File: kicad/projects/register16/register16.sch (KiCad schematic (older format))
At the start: 42 parts, among them J1 INPUT_ENABLE, J10 LOW, J2 OUTPUT_ENABLE, J3 CONTENTS, J4 Control_signal_backplane, J5 Aux_connection, J6 Bus_connection, J7 HIGH, J8 LOW, J9 HIGH, U1 74HCT04, U2 74HCT377, U3 74HCT377, U4 74HCT245, U5 74HCT245, U6 74HCT245, U7 74HCT245

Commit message: Register mostly complete
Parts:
- D1, D10, D11, D12, D13, D14, D15, D16, D2, D3, D4, D5, D6, D7, D8, D9: footprint LED_THT:LED_D5.0mm_Horizontal_O3.81mm_Z3.0mm -> eight-bit-computer:LED_D5.0mm_Horizontal_O3.81mm_Z3.0mm
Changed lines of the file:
@@
 F 0 "D15" H 8500 2850 50  0000 C CNN
 F 1 "LED" H 8300 2850 50  0000 C CNN
-F 2 "LED_THT:LED_D5.0mm_Horizontal_O3.81mm_Z3.0mm" H 8750 2900 50  0001 C CNN
+F 2 "eight-bit-computer:LED_D5.0mm_Horizontal_O3.81mm_Z3.0mm" H 8750 2900 50  0001 C CNN
 F 3 "~" H 8750 2900 50  0001 C CNN
 	1    8750 2900
@@
 F 0 "D16" H 8500 3000 50  0000 C CNN
 F 1 "LED" H 8300 3000 50  0000 C CNN
-F 2 "LED_THT:LED_D5.0mm_Horizontal_O3.81mm_Z3.0mm" H 8750 3050 50  0001 C CNN
+F 2 "eight-bit-computer:LED_D5.0mm_Horizontal_O3.81mm_Z3.0mm" H 8750 3050 50  0001 C CNN
 F 3 "~" H 8750 3050 50  0001 C CNN
 	1    8750 3050
@@
 F 0 "D13" H 8500 2550 50  0000 C CNN
 F 1 "LED" H 8300 2550 50  0000 C CNN
-F 2 "LED_THT:LED_D5.0mm_Horizontal_O3.81mm_Z3.0mm" H 8750 2600 50  0001 C CNN
+F 2 "eight-bit-computer:LED_D5.0mm_Horizontal_O3.81mm_Z3.0mm" H 8750 2600 50  0001 C CNN
 F 3 "~" H 8750 2600 50  0001 C CNN
 	1    8750 2600
@@
 F 0 "D14" H 8500 2700 50  0000 C CNN
 F 1 "LED" H 8300 2700 50  0000 C CNN
-F 2 "LED_THT:LED_D5.0mm_Horizontal_O3.81mm_Z3.0mm" H 8750 2750 50  0001 C CNN
+F 2 "eight-bit-computer:LED_D5.0mm_Horizontal_O3.81mm_Z3.0mm" H 8750 2750 50  0001 C CNN
 F 3 "~" H 8750 2750 50  0001 C CNN
 	1    8750 2750
@@
 F 0 "D11" H 8500 2250 50  0000 C CNN
 F 1 "LED" H 8300 2250 50  0000 C CNN
-F 2 "LED_THT:LED_D5.0mm_Horizontal_O3.81mm_Z3.0mm" H 8750 2300 50  0001 C CNN
+F 2 "eight-bit-computer:LED_D5.0mm_Horizontal_O3.81mm_Z3.0mm" H 8750 2300 50  0001 C CNN
 F 3 "~" H 8750 2300 50  0001 C CNN
 	1    8750 2300
@@
 F 0 "D12" H 8500 2400 50  0000 C CNN
 F 1 "LED" H 8300 2400 50  0000 C CNN
-F 2 "LED_THT:LED_D5.0mm_Horizontal_O3.81mm_Z3.0mm" H 8750 2450 50  0001 C CNN
+F 2 "eight-bit-computer:LED_D5.0mm_Horizontal_O3.81mm_Z3.0mm" H 8750 2450 50  0001 C CNN
 F 3 "~" H 8750 2450 50  0001 C CNN
 	1    8750 2450
@@
 F 0 "D9" H 8500 1950 50  0000 C CNN
 F 1 "LED" H 8300 1950 50  0000 C CNN
-F 2 "LED_THT:LED_D5.0mm_Horizontal_O3.81mm_Z3.0mm" H 8750 2000 50  0001 C CNN
+F 2 "eight-bit-computer:LED_D5.0mm_Horizontal_O3.81mm_Z3.0mm" H 8750 2000 50  0001 C CNN
 F 3 "~" H 8750 2000 50  0001 C CNN
 	1    8750 2000
@@
 F 0 "D10" H 8500 2100 50  0000 C CNN
 F 1 "LED" H 8300 2100 50  0000 C CNN
-F 2 "LED_THT:LED_D5.0mm_Horizontal_O3.81mm_Z3.0mm" H 8750 2150 50  0001 C CNN
+F 2 "eight-bit-computer:LED_D5.0mm_Horizontal_O3.81mm_Z3.0mm" H 8750 2150 50  0001 C CNN
 F 3 "~" H 8750 2150 50  0001 C CNN
 	1    8750 2150
@@
 F 0 "D7" H 8500 1650 50  0000 C CNN
 F 1 "LED" H 8300 1650 50  0000 C CNN
-F 2 "LED_THT:LED_D5.0mm_Horizontal_O3.81mm_Z3.0mm" H 8750 1700 50  0001 C CNN
+F 2 "eight-bit-computer:LED_D5.0mm_Horizontal_O3.81mm_Z3.0mm" H 8750 1700 50  0001 C CNN
 F 3 "~" H 8750 1700 50  0001 C CNN
 	1    8750 1700
@@
 F 0 "D8" H 8500 1800 50  0000 C CNN
 F 1 "LED" H 8300 1800 50  0000 C CNN
-F 2 "LED_THT:LED_D5.0mm_Horizontal_O3.81mm_Z3.0mm" H 8750 1850 50  0001 C CNN
+F 2 "eight-bit-computer:LED_D5.0mm_Horizontal_O3.81mm_Z3.0mm" H 8750 1850 50  0001 C CNN
 F 3 "~" H 8750 1850 50  0001 C CNN
 	1    8750 1850
@@
 F 0 "D5" H 8500 1350 50  0000 C CNN
 F 1 "LED" H 8300 1350 50  0000 C CNN
-F 2 "LED_THT:LED_D5.0mm_Horizontal_O3.81mm_Z3.0mm" H 8750 1400 50  0001 C CNN
+F 2 "eight-bit-computer:LED_D5.0mm_Horizontal_O3.81mm_Z3.0mm" H 8750 1400 50  0001 C CNN
 F 3 "~" H 8750 1400 50  0001 C CNN
 	1    8750 1400
@@
 F 0 "D6" H 8500 1500 50  0000 C CNN
 F 1 "LED" H 8300 1500 50  0000 C CNN
-F 2 "LED_THT:LED_D5.0mm_Horizontal_O3.81mm_Z3.0mm" H 8750 1550 50  0001 C CNN
+F 2 "eight-bit-computer:LED_D5.0mm_Horizontal_O3.81mm_Z3.0mm" H 8750 1550 50  0001 C CNN
 F 3 "~" H 8750 1550 50  0001 C CNN
 	1    8750 1550
@@
 F 0 "D3" H 8500 1050 50  0000 C CNN
 F 1 "LED" H 8300 1050 50  0000 C CNN
-F 2 "LED_THT:LED_D5.0mm_Horizontal_O3.81mm_Z3.0mm" H 8750 1100 50  0001 C CNN
+F 2 "eight-bit-computer:LED_D5.0mm_Horizontal_O3.81mm_Z3.0mm" H 8750 1100 50  0001 C CNN
 F 3 "~" H 8750 1100 50  0001 C CNN
 	1    8750 1100
@@
 F 0 "D4" H 8500 1200 50  0000 C CNN
 F 1 "LED" H 8300 1200 50  0000 C CNN
-F 2 "LED_THT:LED_D5.0mm_Horizontal_O3.81mm_Z3.0mm" H 8750 1250 50  0001 C CNN
+F 2 "eight-bit-computer:LED_D5.0mm_Horizontal_O3.81mm_Z3.0mm" H 8750 1250 50  0001 C CNN
 F 3 "~" H 8750 1250 50  0001 C CNN
 	1    8750 1250
@@
 F 0 "D1" H 8500 750 50  0000 C CNN
 F 1 "LED" H 8300 750 50  0000 C CNN
-F 2 "LED_THT:LED_D5.0mm_Horizontal_O3.81mm_Z3.0mm" H 8750 800 50  0001 C CNN
+F 2 "eight-bit-computer:LED_D5.0mm_Horizontal_O3.81mm_Z3.0mm" H 8750 800 50  0001 C CNN
 F 3 "~" H 8750 800 50  0001 C CNN
 	1    8750 800
@@
 F 0 "D2" H 8500 900 50  0000 C CNN
 F 1 "LED" H 8300 900 50  0000 C CNN
-F 2 "LED_THT:LED_D5.0mm_Horizontal_O3.81mm_Z3.0mm" H 8750 950 50  0001 C CNN
+F 2 "eight-bit-computer:LED_D5.0mm_Horizontal_O3.81mm_Z3.0mm" H 8750 950 50  0001 C CNN
 F 3 "~" H 8750 950 50  0001 C CNN
 	1    8750 950

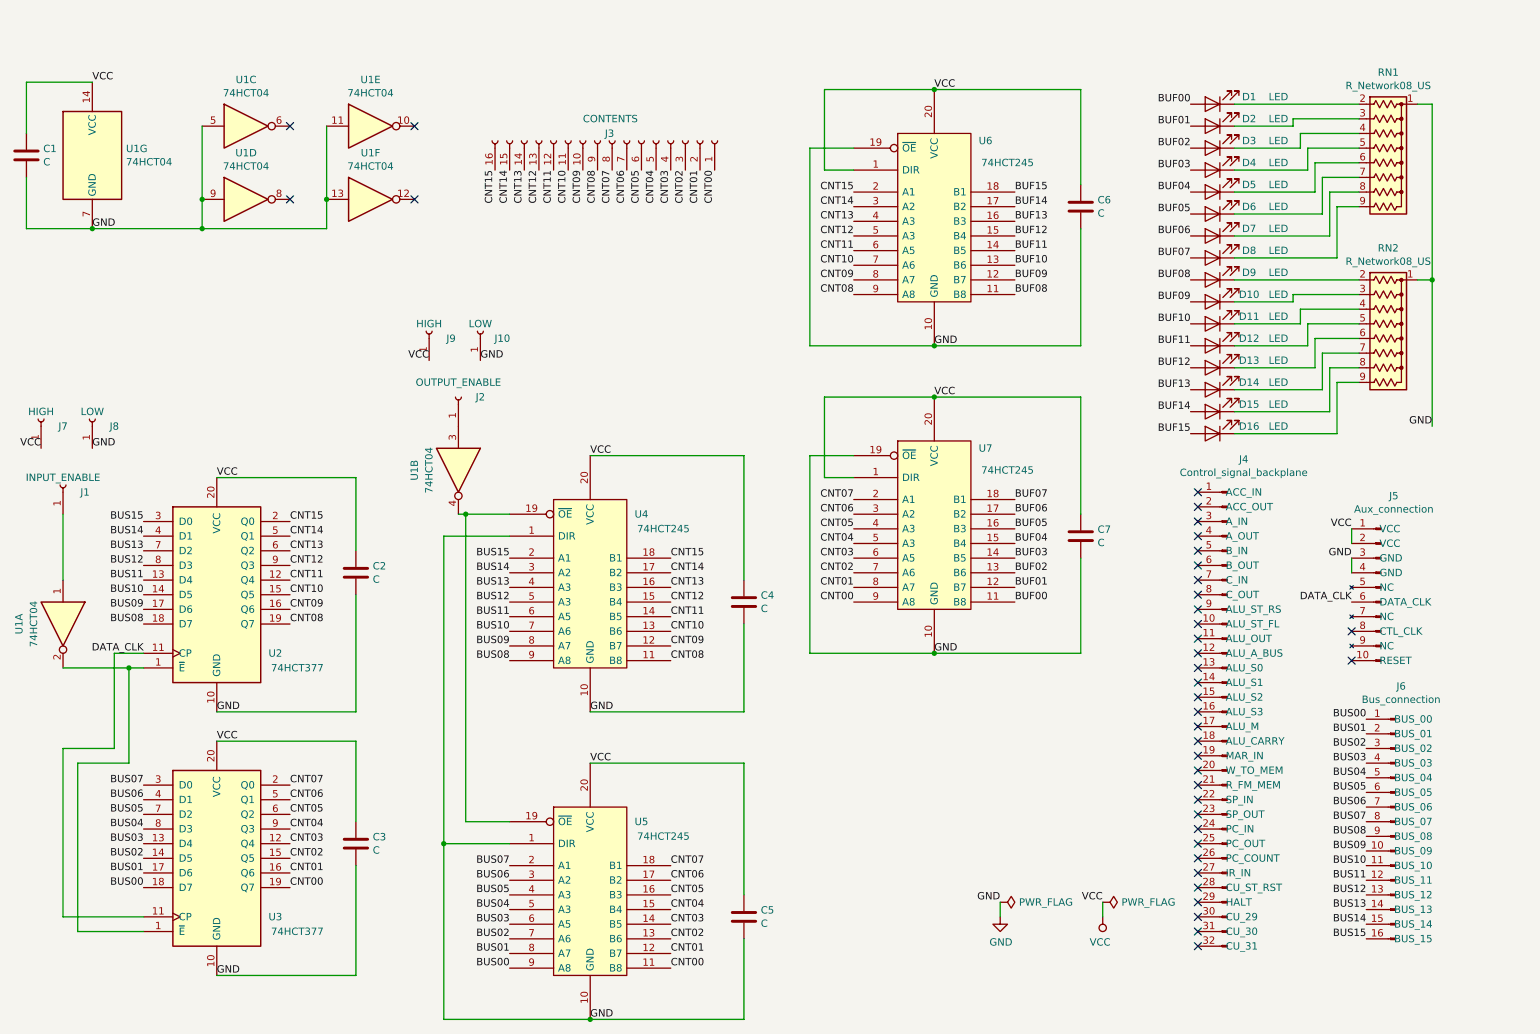
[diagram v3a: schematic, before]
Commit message: Add aux and bus footprints. Tidy up in register. Add power cap to reg.
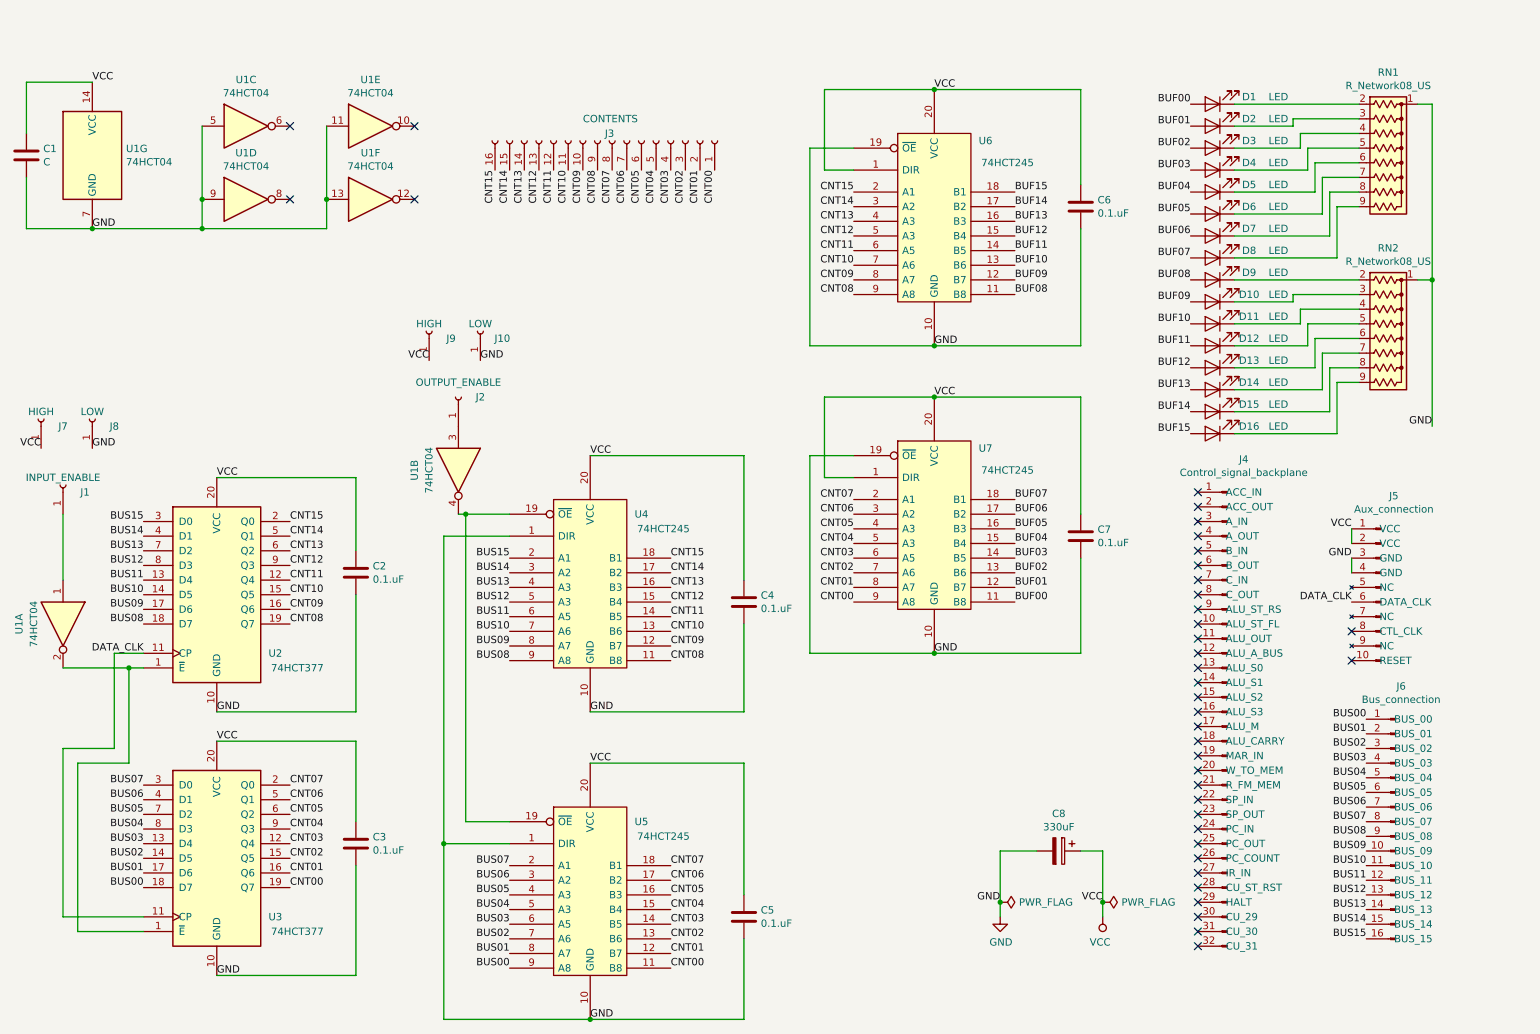
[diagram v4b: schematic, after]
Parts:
- added C8: 330uF, Capacitor_THT:CP_Radial_D6.3mm_P2.50mm, symbol Device:CP
- C2, C3, C4, C5, C6, C7: value C -> 0.1.uF
- J4: footprint eight-bit-computer:backplane-connector -> eight-bit-computer:backplane-connector-annotated
- J5: footprint Connector_PinHeader_2.54mm:PinHeader_1x10_P2.54mm_Horizontal -> eight-bit-computer:aux-connection
- J6: footprint Connector_PinHeader_2.54mm:PinHeader_1x16_P2.54mm_Horizontal -> eight-bit-computer:bus-connection
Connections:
- net GND: now also C8.2
- net VCC: now also C8.1
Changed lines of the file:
@@
 F 0 "J5" H 9812 4725 50  0000 C CNN
 F 1 "Aux_connection" H 9812 4634 50  0000 C CNN
-F 2 "Connector_PinHeader_2.54mm:PinHeader_1x10_P2.54mm_Horizontal" H 9900 4100 50  0001 C CNN
+F 2 "eight-bit-computer:aux-connection" H 9900 4100 50  0001 C CNN
 F 3 "~" H 9900 4100 50  0001 C CNN
 	1    9900 4100
@@
 F 0 "J6" H 9762 6625 50  0000 C CNN
 F 1 "Bus_connection" H 9762 6534 50  0000 C CNN
-F 2 "Connector_PinHeader_2.54mm:PinHeader_1x16_P2.54mm_Horizontal" H 9800 6100 50  0001 C CNN
+F 2 "eight-bit-computer:bus-connection" H 9800 6100 50  0001 C CNN
 F 3 "~" H 9800 6100 50  0001 C CNN
 	1    9900 5700
@@
 F 0 "J4" H 8737 6675 50  0000 C CNN
 F 1 "Control_signal_backplane" H 8737 6584 50  0000 C CNN
-F 2 "eight-bit-computer:backplane-connector" H 8850 4950 50  0001 C CNN
+F 2 "eight-bit-computer:backplane-connector-annotated" H 8850 4950 50  0001 C CNN
 F 3 "~" H 8850 4950 50  0001 C CNN
 	1    8850 4950
@@
 P 7850 3750
 F 0 "C7" H 7965 3796 50  0000 L CNN
-F 1 "C" H 7965 3705 50  0000 L CNN
+F 1 "0.1.uF" H 7965 3705 50  0000 L CNN
 F 2 "Capacitor_THT:C_Disc_D4.3mm_W1.9mm_P5.00mm" H 7888 3600 50  0001 C CNN
 F 3 "~" H 7850 3750 50  0001 C CNN
@@
 P 7850 1500
 F 0 "C6" H 7965 1546 50  0000 L CNN
-F 1 "C" H 7965 1455 50  0000 L CNN
+F 1 "0.1.uF" H 7965 1455 50  0000 L CNN
 F 2 "Capacitor_THT:C_Disc_D4.3mm_W1.9mm_P5.00mm" H 7888 1350 50  0001 C CNN
 F 3 "~" H 7850 1500 50  0001 C CNN
@@
 P 5550 4200
 F 0 "C4" H 5665 4246 50  0000 L CNN
-F 1 "C" H 5665 4155 50  0000 L CNN
+F 1 "0.1.uF" H 5665 4155 50  0000 L CNN
 F 2 "Capacitor_THT:C_Disc_D4.3mm_W1.9mm_P5.00mm" H 5588 4050 50  0001 C CNN
 F 3 "~" H 5550 4200 50  0001 C CNN
@@
 P 5550 6350
 F 0 "C5" H 5665 6396 50  0000 L CNN
-F 1 "C" H 5665 6305 50  0000 L CNN
+F 1 "0.1.uF" H 5665 6305 50  0000 L CNN
 F 2 "Capacitor_THT:C_Disc_D4.3mm_W1.9mm_P5.00mm" H 5588 6200 50  0001 C CNN
 F 3 "~" H 5550 6350 50  0001 C CNN
@@
 P 2900 5850
 F 0 "C3" H 3015 5896 50  0000 L CNN
-F 1 "C" H 3015 5805 50  0000 L CNN
+F 1 "0.1.uF" H 3015 5805 50  0000 L CNN
 F 2 "Capacitor_THT:C_Disc_D4.3mm_W1.9mm_P5.00mm" H 2938 5700 50  0001 C CNN
 F 3 "~" H 2900 5850 50  0001 C CNN
@@
 P 2900 4000
 F 0 "C2" H 3015 4046 50  0000 L CNN
-F 1 "C" H 3015 3955 50  0000 L CNN
+F 1 "0.1.uF" H 3015 3955 50  0000 L CNN
 F 2 "Capacitor_THT:C_Disc_D4.3mm_W1.9mm_P5.00mm" H 2938 3850 50  0001 C CNN
 F 3 "~" H 2900 4000 50  0001 C CNN
@@
 	1    0    0    -1
 $EndComp
+$Comp
+L Device:CP C8
+U 1 1 5FBE440D
+P 7700 5900
+F 0 "C8" V 7445 5900 50  0000 C CNN
+F 1 "330uF" V 7536 5900 50  0000 C CNN
+F 2 "Capacitor_THT:CP_Radial_D6.3mm_P2.50mm" H 7738 5750 50  0001 C CNN
+F 3 "~" H 7700 5900 50  0001 C CNN
+	1    7700 5900
+	0    1    1    0
+$EndComp
+Wire Wire Line
+	7550 5900 7300 5900
+Wire Wire Line
+	7300 5900 7300 6250
+Connection ~ 7300 6250
+Wire Wire Line
+	7850 5900 8000 5900
+Wire Wire Line
+	8000 5900 8000 6250
+Connection ~ 8000 6250
 $EndSCHEMATC

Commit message: Finishing touches to Register
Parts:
- C1: value C -> 0.1uF
- C2, C3, C4, C5, C6, C7: value 0.1.uF -> 0.1uF
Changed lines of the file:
@@
 P 7850 3750
 F 0 "C7" H 7965 3796 50  0000 L CNN
-F 1 "0.1.uF" H 7965 3705 50  0000 L CNN
+F 1 "0.1uF" H 7965 3705 50  0000 L CNN
 F 2 "Capacitor_THT:C_Disc_D4.3mm_W1.9mm_P5.00mm" H 7888 3600 50  0001 C CNN
 F 3 "~" H 7850 3750 50  0001 C CNN
@@
 P 7850 1500
 F 0 "C6" H 7965 1546 50  0000 L CNN
-F 1 "0.1.uF" H 7965 1455 50  0000 L CNN
+F 1 "0.1uF" H 7965 1455 50  0000 L CNN
 F 2 "Capacitor_THT:C_Disc_D4.3mm_W1.9mm_P5.00mm" H 7888 1350 50  0001 C CNN
 F 3 "~" H 7850 1500 50  0001 C CNN
@@
 P 5550 4200
 F 0 "C4" H 5665 4246 50  0000 L CNN
-F 1 "0.1.uF" H 5665 4155 50  0000 L CNN
+F 1 "0.1uF" H 5665 4155 50  0000 L CNN
 F 2 "Capacitor_THT:C_Disc_D4.3mm_W1.9mm_P5.00mm" H 5588 4050 50  0001 C CNN
 F 3 "~" H 5550 4200 50  0001 C CNN
@@
 P 5550 6350
 F 0 "C5" H 5665 6396 50  0000 L CNN
-F 1 "0.1.uF" H 5665 6305 50  0000 L CNN
+F 1 "0.1uF" H 5665 6305 50  0000 L CNN
 F 2 "Capacitor_THT:C_Disc_D4.3mm_W1.9mm_P5.00mm" H 5588 6200 50  0001 C CNN
 F 3 "~" H 5550 6350 50  0001 C CNN
@@
 P 2900 5850
 F 0 "C3" H 3015 5896 50  0000 L CNN
-F 1 "0.1.uF" H 3015 5805 50  0000 L CNN
+F 1 "0.1uF" H 3015 5805 50  0000 L CNN
 F 2 "Capacitor_THT:C_Disc_D4.3mm_W1.9mm_P5.00mm" H 2938 5700 50  0001 C CNN
 F 3 "~" H 2900 5850 50  0001 C CNN
@@
 P 2900 4000
 F 0 "C2" H 3015 4046 50  0000 L CNN
-F 1 "0.1.uF" H 3015 3955 50  0000 L CNN
+F 1 "0.1uF" H 3015 3955 50  0000 L CNN
 F 2 "Capacitor_THT:C_Disc_D4.3mm_W1.9mm_P5.00mm" H 2938 3850 50  0001 C CNN
 F 3 "~" H 2900 4000 50  0001 C CNN
@@
 P 650 1150
 F 0 "C1" H 765 1196 50  0000 L CNN
-F 1 "C" H 765 1105 50  0000 L CNN
+F 1 "0.1uF" H 765 1105 50  0000 L CNN
 F 2 "Capacitor_THT:C_Disc_D4.3mm_W1.9mm_P5.00mm" H 688 1000 50  0001 C CNN
 F 3 "~" H 650 1150 50  0001 C CNN

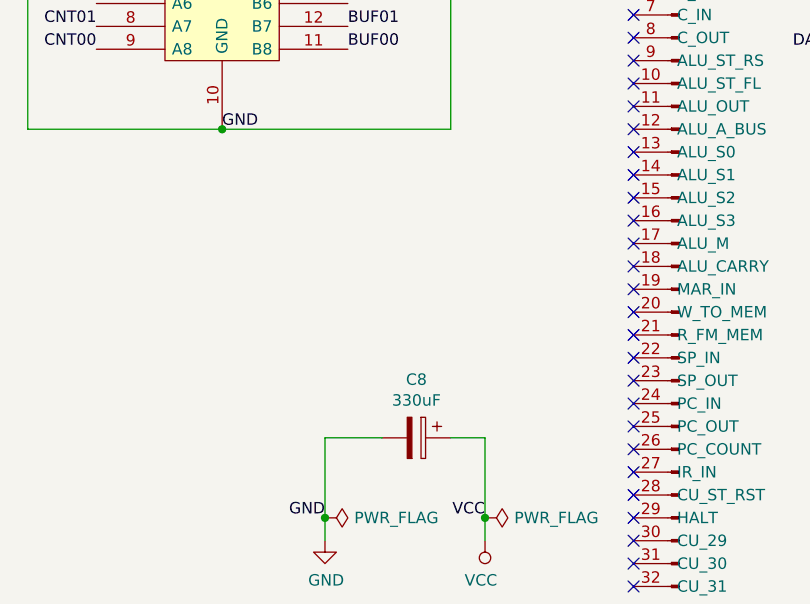
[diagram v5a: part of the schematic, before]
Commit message: Added more large caps, shrunk vias a bit
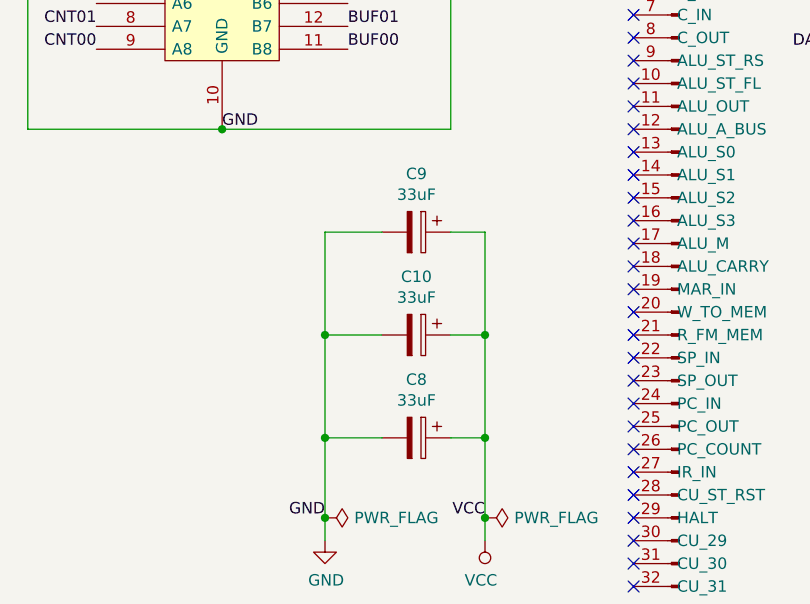
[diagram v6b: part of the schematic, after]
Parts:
- added C10, C9: 33uF, Capacitor_THT:CP_Radial_D6.3mm_P2.50mm, symbol Device:CP
- C8: value 330uF -> 33uF
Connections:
- net GND: now also C10.2, C9.2
- net VCC: now also C10.1, C9.1
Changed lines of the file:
@@
 P 7700 5900
 F 0 "C8" V 7445 5900 50  0000 C CNN
-F 1 "330uF" V 7536 5900 50  0000 C CNN
+F 1 "33uF" V 7536 5900 50  0000 C CNN
 F 2 "Capacitor_THT:CP_Radial_D6.3mm_P2.50mm" H 7738 5750 50  0001 C CNN
 F 3 "~" H 7700 5900 50  0001 C CNN
@@
 	8000 5900 8000 6250
 Connection ~ 8000 6250
+$Comp
+L Device:CP C10
+U 1 1 5FC5AD3A
+P 7700 5450
+F 0 "C10" V 7445 5450 50  0000 C CNN
+F 1 "33uF" V 7536 5450 50  0000 C CNN
+F 2 "Capacitor_THT:CP_Radial_D6.3mm_P2.50mm" H 7738 5300 50  0001 C CNN
+F 3 "~" H 7700 5450 50  0001 C CNN
+	1    7700 5450
+	0    1    1    0
+$EndComp
+$Comp
+L Device:CP C9
+U 1 1 5FC5B53A
+P 7700 5000
+F 0 "C9" V 7445 5000 50  0000 C CNN
+F 1 "33uF" V 7536 5000 50  0000 C CNN
+F 2 "Capacitor_THT:CP_Radial_D6.3mm_P2.50mm" H 7738 4850 50  0001 C CNN
+F 3 "~" H 7700 5000 50  0001 C CNN
+	1    7700 5000
+	0    1    1    0
+$EndComp
+Wire Wire Line
+	7300 5900 7300 5450
+Wire Wire Line
+	7300 5450 7550 5450
+Connection ~ 7300 5900
+Wire Wire Line
+	7300 5450 7300 5000
+Wire Wire Line
+	7300 5000 7550 5000
+Connection ~ 7300 5450
+Wire Wire Line
+	7850 5000 8000 5000
+Wire Wire Line
+	8000 5000 8000 5450
+Connection ~ 8000 5900
+Wire Wire Line
+	7850 5450 8000 5450
+Connection ~ 8000 5450
+Wire Wire Line
+	8000 5450 8000 5900
 $EndSCHEMATC
